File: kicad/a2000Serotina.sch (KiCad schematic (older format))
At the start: 23 parts

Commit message: Further work on Keyboard Matrix
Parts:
- added D13, D14, D15, D16, D17, D18, D19, D20, D21, D22, D23, D24, D25, D26, D27, D28, D29, D30, D31, D32, D33, D34, D35, D36, D37, D38, D39, D40, D41, D42, D43, D44, D45, D46, D47, D48, D49, D50, D51, D52, D53, D54, D55, D56, D57, D58, D59, D60, D61, D62, D63, D64, D65, D66, D67, D68, D69, D70, D8: D_Small, symbol Device:D_Small
- added MX13, MX14, MX15, MX16, MX17, MX18, MX19, MX20, MX21, MX22, MX23, MX24, MX25, MX26, MX27, MX28, MX29, MX30, MX31, MX32, MX33, MX34, MX35, MX36, MX37, MX38, MX39, MX40, MX41, MX42, MX43, MX44, MX45, MX46, MX47, MX48, MX49, MX50, MX51, MX52, MX53, MX54, MX55, MX56, MX57, MX58, MX59, MX60, MX61, MX62, MX63, MX64, MX65, MX66, MX67, MX68, MX69, MX70, MX8: MX-NoLED, symbol MX_Alps_Hybrid:MX-NoLED
- renumbered D9 to D10, D10 to D11, D11 to D12, D8 to D9, MX9 to MX10, MX10 to MX11, MX11 to MX12, MX8 to MX9
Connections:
- net COL0: no longer MX1.1 (COL)
- net ROW0: no longer D1.1 (K)
- net ROW1: no longer D2.1 (K)
- net ROW10: no longer D11.1 (K)
- net ROW11: no longer D12.1 (K)
- net ROW3: no longer D3.1 (K)
- net ROW4: no longer D4.1 (K)
- net ROW5: no longer D5.1 (K)
- net ROW6: no longer D6.1 (K)
- net ROW7: no longer D7.1 (K)
- net ROW8: no longer D9.1 (K)
- net ROW9: no longer D10.1 (K)
- new net: D13.2 (A), MX13.2 (ROW)
- new net: D14.2 (A), MX14.2 (ROW)
- new net: D15.2 (A), MX15.2 (ROW)
- new net: D16.2 (A), MX16.2 (ROW)
- new net: D17.2 (A), MX17.2 (ROW)
- new net: D19.2 (A), MX19.2 (ROW)
- new net: D20.2 (A), MX20.2 (ROW)
- new net: D21.2 (A), MX21.2 (ROW)
- new net: D22.2 (A), MX22.2 (ROW)
- new net: D25.2 (A), MX25.2 (ROW)
- new net: D24.2 (A), MX24.2 (ROW)
- new net: D23.2 (A), MX23.2 (ROW)
- new net: D26.2 (A), MX26.2 (ROW)
- new net: D27.2 (A), MX27.2 (ROW)
- new net: D28.2 (A), MX28.2 (ROW)
- new net: D29.2 (A), MX29.2 (ROW)
- new net: D30.2 (A), MX30.2 (ROW)
- new net: D31.2 (A), MX31.2 (ROW)
- new net: D18.2 (A), MX18.2 (ROW)
- new net: D8.2 (A), MX8.2 (ROW)
- new net: D32.2 (A), MX32.2 (ROW)
- new net: D33.2 (A), MX33.2 (ROW)
- new net: D34.2 (A), MX34.2 (ROW)
- new net: D35.2 (A), MX35.2 (ROW)
- new net: D36.2 (A), MX36.2 (ROW)
- new net: D37.2 (A), MX37.2 (ROW)
- new net: D38.2 (A), MX38.2 (ROW)
- new net: D39.2 (A), MX39.2 (ROW)
- new net: D40.2 (A), MX40.2 (ROW)
- new net: D41.2 (A), MX41.2 (ROW)
- new net: D42.2 (A), MX42.2 (ROW)
- new net: D43.2 (A), MX43.2 (ROW)
- new net: D44.2 (A), MX44.2 (ROW)
- new net: D45.2 (A), MX45.2 (ROW)
- new net: D46.2 (A), MX46.2 (ROW)
- new net: D47.2 (A), MX47.2 (ROW)
- new net: D48.2 (A), MX48.2 (ROW)
- new net: D49.2 (A), MX49.2 (ROW)
- new net: D50.2 (A), MX50.2 (ROW)
- new net: D51.2 (A), MX51.2 (ROW)
- new net: D52.2 (A), MX52.2 (ROW)
- new net: D53.2 (A), MX53.2 (ROW)
- new net: D54.2 (A), MX54.2 (ROW)
- new net: D55.2 (A), MX55.2 (ROW)
- new net: D56.2 (A), MX56.2 (ROW)
- new net: D57.2 (A), MX57.2 (ROW)
- new net: D58.2 (A), MX58.2 (ROW)
- new net: D59.2 (A), MX59.2 (ROW)
- new net: D60.2 (A), MX60.2 (ROW)
- new net: D61.2 (A), MX61.2 (ROW)
- new net: D62.2 (A), MX62.2 (ROW)
- new net: D63.2 (A), MX63.2 (ROW)
- new net: D64.2 (A), MX64.2 (ROW)
- new net: D65.2 (A), MX65.2 (ROW)
- new net: D66.2 (A), MX66.2 (ROW)
- new net: D67.2 (A), MX67.2 (ROW)
- new net: D68.2 (A), MX68.2 (ROW)
- new net: D69.2 (A), MX69.2 (ROW)
- new net: D70.2 (A), MX70.2 (ROW)
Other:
- moved on the sheet: D10, D11, D12, D7, D9, MX10, MX11, MX12, MX7, MX9

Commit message: Matrix now complete.
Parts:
- added D100, D101, D102, D103, D104, D105, D71, D72, D73, D74, D75, D76, D77, D78, D79, D80, D81, D82, D83, D84, D85, D86, D87, D88, D89, D90, D91, D92, D93, D94, D95, D96, D97, D98, D99: D_Small, symbol Device:D_Small
- added MX100, MX101, MX102, MX103, MX104, MX105, MX71, MX72, MX73, MX74, MX75, MX76, MX77, MX78, MX79, MX80, MX81, MX82, MX83, MX84, MX85, MX86, MX87, MX88, MX89, MX90, MX91, MX92, MX93, MX94, MX95, MX96, MX97, MX98, MX99: MX-NoLED, symbol MX_Alps_Hybrid:MX-NoLED
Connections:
- net COL0: now also MX1.1 (COL), MX10.1 (COL), MX11.1 (COL), MX12.1 (COL), MX2.1 (COL), MX3.1 (COL), MX4.1 (COL), MX5.1 (COL), MX6.1 (COL), MX7.1 (COL), MX8.1 (COL), MX9.1 (COL)
- net COL1: now also MX13.1 (COL), MX14.1 (COL), MX15.1 (COL), MX16.1 (COL), MX17.1 (COL), MX18.1 (COL), MX19.1 (COL), MX20.1 (COL), MX21.1 (COL), MX22.1 (COL)
- net COL10: now also MX104.1 (COL), MX105.1 (COL)
- net COL2: now also MX23.1 (COL), MX24.1 (COL), MX25.1 (COL), MX26.1 (COL), MX27.1 (COL), MX28.1 (COL), MX29.1 (COL), MX30.1 (COL), MX31.1 (COL), MX32.1 (COL), MX33.1 (COL), MX34.1 (COL)
- net COL3: now also MX35.1 (COL), MX36.1 (COL), MX37.1 (COL), MX38.1 (COL), MX39.1 (COL), MX40.1 (COL), MX41.1 (COL), MX42.1 (COL), MX43.1 (COL), MX44.1 (COL), MX45.1 (COL), MX46.1 (COL)
- net COL4: now also MX47.1 (COL), MX48.1 (COL), MX49.1 (COL), MX50.1 (COL), MX51.1 (COL), MX52.1 (COL), MX53.1 (COL), MX54.1 (COL), MX55.1 (COL), MX56.1 (COL), MX57.1 (COL), MX58.1 (COL)
- net COL5: now also MX59.1 (COL), MX60.1 (COL), MX61.1 (COL), MX62.1 (COL), MX63.1 (COL), MX64.1 (COL), MX65.1 (COL), MX66.1 (COL), MX67.1 (COL), MX68.1 (COL), MX69.1 (COL), MX70.1 (COL)
- net COL6: now also MX71.1 (COL), MX72.1 (COL), MX73.1 (COL), MX74.1 (COL), MX75.1 (COL), MX76.1 (COL), MX77.1 (COL), MX78.1 (COL), MX79.1 (COL)
- net COL7: now also MX80.1 (COL), MX81.1 (COL), MX82.1 (COL), MX83.1 (COL), MX84.1 (COL), MX85.1 (COL), MX86.1 (COL), MX87.1 (COL), MX88.1 (COL), MX89.1 (COL)
- net COL8: now also MX90.1 (COL), MX91.1 (COL), MX92.1 (COL), MX93.1 (COL), MX94.1 (COL), MX95.1 (COL)
- net COL9: now also MX100.1 (COL), MX101.1 (COL), MX102.1 (COL), MX103.1 (COL), MX98.1 (COL), MX99.1 (COL)
- net ROW0: now also D1.1 (K), D23.1 (K), D35.1 (K), D47.1 (K), D59.1 (K), D80.1 (K), D90.1 (K), D98.1 (K)
- net ROW1: now also D2.1 (K), D24.1 (K), D36.1 (K), D48.1 (K), D60.1 (K), D81.1 (K), D91.1 (K), D99.1 (K)
- net ROW10: now also D11.1 (K), D21.1 (K), D33.1 (K), D45.1 (K), D57.1 (K), D69.1 (K), D79.1 (K)
- net ROW11: now also D12.1 (K), D22.1 (K), D34.1 (K), D46.1 (K), D58.1 (K), D70.1 (K)
- net ROW2: now also D13.1 (K), D25.1 (K), D3.1 (K), D37.1 (K), D49.1 (K), D61.1 (K), D100.1 (K), D104.1 (K), D71.1 (K), D82.1 (K), D92.1 (K)
- net ROW3: now also D14.1 (K), D26.1 (K), D38.1 (K), D4.1 (K), D50.1 (K), D62.1 (K), D101.1 (K), D72.1 (K), D83.1 (K), D93.1 (K)
- net ROW4: now also D15.1 (K), D27.1 (K), D39.1 (K), D5.1 (K), D51.1 (K), D63.1 (K), D102.1 (K), D105.1 (K), D73.1 (K), D84.1 (K), D94.1 (K)
- net ROW5: now also D16.1 (K), D28.1 (K), D40.1 (K), D52.1 (K), D6.1 (K), D64.1 (K), D103.1 (K), D74.1 (K), D85.1 (K), D95.1 (K)
- net ROW6: now also D17.1 (K), D29.1 (K), D41.1 (K), D53.1 (K), D65.1 (K), D7.1 (K), D75.1 (K), D86.1 (K)
- net ROW7: now also D18.1 (K), D30.1 (K), D42.1 (K), D54.1 (K), D66.1 (K), D8.1 (K), D76.1 (K), D87.1 (K)
- net ROW8: now also D19.1 (K), D31.1 (K), D43.1 (K), D55.1 (K), D67.1 (K), D9.1 (K), D77.1 (K), D88.1 (K), D96.1 (K)
- net ROW9: now also D10.1 (K), D20.1 (K), D32.1 (K), D44.1 (K), D56.1 (K), D68.1 (K), D78.1 (K), D89.1 (K), D97.1 (K)
- new net: D71.2 (A), MX71.2 (ROW)
- new net: D72.2 (A), MX72.2 (ROW)
- new net: D73.2 (A), MX73.2 (ROW)
- new net: D74.2 (A), MX74.2 (ROW)
- new net: D75.2 (A), MX75.2 (ROW)
- new net: D76.2 (A), MX76.2 (ROW)
- new net: D77.2 (A), MX77.2 (ROW)
- new net: D78.2 (A), MX78.2 (ROW)
- new net: D79.2 (A), MX79.2 (ROW)
- new net: D80.2 (A), MX80.2 (ROW)
- new net: D81.2 (A), MX81.2 (ROW)
- new net: D82.2 (A), MX82.2 (ROW)
- new net: D83.2 (A), MX83.2 (ROW)
- new net: D84.2 (A), MX84.2 (ROW)
- new net: D85.2 (A), MX85.2 (ROW)
- new net: D86.2 (A), MX86.2 (ROW)
- new net: D87.2 (A), MX87.2 (ROW)
- new net: D88.2 (A), MX88.2 (ROW)
- new net: D89.2 (A), MX89.2 (ROW)
- new net: D90.2 (A), MX90.2 (ROW)
- new net: D91.2 (A), MX91.2 (ROW)
- new net: D92.2 (A), MX92.2 (ROW)
- new net: D93.2 (A), MX93.2 (ROW)
- new net: D94.2 (A), MX94.2 (ROW)
- new net: D95.2 (A), MX95.2 (ROW)
- new net: D96.2 (A), MX96.2 (ROW)
- new net: D97.2 (A), MX97.2 (ROW)
- new net: D98.2 (A), MX98.2 (ROW)
- new net: D99.2 (A), MX99.2 (ROW)
- new net: D100.2 (A), MX100.2 (ROW)
- new net: D101.2 (A), MX101.2 (ROW)
- new net: D102.2 (A), MX102.2 (ROW)
- new net: D103.2 (A), MX103.2 (ROW)
- new net: D104.2 (A), MX104.2 (ROW)
- new net: D105.2 (A), MX105.2 (ROW)
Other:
- moved on the sheet: D8, MX8

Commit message: Connections and wiring complete
Now working on PCB Footprints.
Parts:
- removed MX11, MX33, MX69: MX-NoLED, symbol MX_Alps_Hybrid:MX-NoLED
- added J1: KCDX-5S-S2, SamacSys_Parts:KCDX5SS2, symbol SamacSys_Parts:KCDX-5S-S2
- added LED1, LED2, LED3, LED4, LED5, LED6, LED7, LED8: LED, LED_THT:LED_D3.0mm, symbol Device:LED
- added MX11, MX33, MX69: MX-LED, symbol MX_Alps_Hybrid:MX-LED
- added R1, R10, R11, R12, R2, R3, R4, R5, R6, R7, R8, R9: 150, Resistor_THT:R_Axial_DIN0207_L6.3mm_D2.5mm_P10.16mm_Horizontal, symbol Device:R_Small
- D1, D10, D100, D101, D102, D103, D104, D105, D11, D12, D13, D14, D15, D16, D17, D18, D19, D2, D20, D21, D22, D23, D24, D25, D26, D27, D28, D29, D3, D30, D31, D32, D33, D34, D35, D36, D37, D38, D39, D4, D40, D41, D42, D43, D44, D45, D46, D47, D48, D49, D5, D50, D51, D52, D53, D54, D55, D56, D57, D58, D59, D6, D60, D61, D62, D63, D64, D65, D66, D67, D68, D69, D7, D70, D71, D72, D73, D74, D75, D76, D77, D78, D79, D8, D80, D81, D82, D83, D84, D85, D86, D87, D88, D89, D9, D90, D91, D92, D93, D94, D95, D96, D97, D98, D99: footprint (none) -> Diode_THT:D_DO-35_SOD27_P7.62mm_Horizontal
- U1: renamed from U?; footprint (none) -> teensy:Teensy2.0++
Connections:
- net COL0: now also MX11.1 (COL)
- net COL2: now also MX33.1 (COL)
- net COL5: now also MX69.1 (COL)
- net COL8: now also MX96.1 (COL), MX97.1 (COL)
- net CPLCK: now also R12.2
- net GND: now also MX7.4 (LEDGND), J1.5, LED1.1 (K), LED2.1 (K), LED3.1 (K), LED4.1 (K), LED5.1 (K), LED6.1 (K), LED7.1 (K), LED8.1 (K), MX11.4 (LEDGND), MX33.4 (LEDGND), MX69.4 (LEDGND)
- net KCLK: now also J1.3, R9.1
- net KDAT: now also J1.2, R10.1
- net NMLCK: now also R7.1
- net SCLCK: now also R8.1
- net STA1: now also R4.1
- net STA2: now also R5.1
- net STA3: now also R6.1
- net VCC: now also J1.4, R11.1
- net LCTRL: now reaches U1.11 (PE0)
- net LCTRL: now also R1.1
- net LALT: now reaches U1.12 (PE1)
- net LALT: now also R2.1
- net RGUI: now reaches U1.2 (PB7_OC0A_OC1C)
- net RGUI: now also R3.1
- net at MX7.3 (LED): now also R12.1
- net at D11.2 (A): now also MX11.2 (ROW)
- net at D33.2 (A): now also MX33.2 (ROW)
- net at D69.2 (A): now also MX69.2 (ROW)
- new net: MX11.3 (LED), R1.2
- new net: MX33.3 (LED), R2.2
- new net: MX69.3 (LED), R3.2
- new net: LED1.2 (A), R4.2
- new net: LED2.2 (A), R5.2
- new net: LED3.2 (A), R6.2
- new net: LED4.2 (A), R7.2
- new net: LED5.2 (A), R8.2
- new net: LED6.2 (A), R9.2
- new net: LED7.2 (A), R10.2
- new net: LED8.2 (A), R11.2

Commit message: All footprints now assigned
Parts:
- MX1, MX10, MX100, MX101, MX102, MX104, MX105, MX13, MX14, MX15, MX16, MX17, MX18, MX19, MX2, MX20, MX22, MX23, MX24, MX25, MX26, MX27, MX28, MX29, MX3, MX30, MX31, MX32, MX34, MX35, MX36, MX37, MX38, MX39, MX4, MX40, MX41, MX42, MX43, MX46, MX47, MX48, MX49, MX50, MX51, MX52, MX53, MX54, MX55, MX56, MX58, MX59, MX6, MX60, MX61, MX62, MX63, MX64, MX65, MX66, MX67, MX68, MX70, MX71, MX72, MX73, MX74, MX75, MX76, MX77, MX78, MX8, MX80, MX81, MX82, MX83, MX84, MX85, MX86, MX87, MX88, MX89, MX90, MX91, MX92, MX93, MX94, MX95, MX96, MX98, MX99: footprint (none) -> MX_Alps_Hybrid:MX-1U-NoLED
- MX103, MX97: footprint (none) -> MX_Alps_Hybrid:MX-2U-NoLED
- MX11, MX33, MX69: footprint (none) -> MX_Alps_Hybrid:MX-1.25U
- MX12, MX21, MX57, MX79, MX9: footprint (none) -> MX_Alps_Hybrid:MX-1.25U-NoLED
- MX44: footprint (none) -> MX_Alps_Hybrid:MX-2.75U-NoLED
- MX45: footprint (none) -> MX_Alps_Hybrid:MX-6.25U-NoLED
- MX5: footprint (none) -> MX_Alps_Hybrid:MX-1.5U-NoLED
- MX7: footprint (none) -> MX_Alps_Hybrid:MX-1.75U

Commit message: Work on PCB Layout
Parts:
- MX26, MX28: footprint MX_Alps_Hybrid:MX-1U-NoLED -> MX_Alps_Hybrid:MX-2U-NoLED
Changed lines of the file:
@@
 F 0 "MX26" H 3383 4071 60  0000 C CNN
 F 1 "MX-NoLED" H 3383 3949 20  0001 C CNN
-F 2 "MX_Alps_Hybrid:MX-1U-NoLED" H 2725 3775 60  0001 C CNN
+F 2 "MX_Alps_Hybrid:MX-2U-NoLED" H 2725 3775 60  0001 C CNN
 F 3 "" H 2725 3775 60  0001 C CNN
 F 4 "BSPC" H 3383 3973 50  0000 C CNN "Key"
@@
 F 0 "MX28" H 3383 5471 60  0000 C CNN
 F 1 "MX-NoLED" H 3383 5349 20  0001 C CNN
-F 2 "MX_Alps_Hybrid:MX-1U-NoLED" H 2725 5175 60  0001 C CNN
+F 2 "MX_Alps_Hybrid:MX-2U-NoLED" H 2725 5175 60  0001 C CNN
 F 3 "" H 2725 5175 60  0001 C CNN
 F 4 "ENT" H 3383 5373 50  0000 C CNN "Key"

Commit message: All switches now placed.
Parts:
- MX58: footprint MX_Alps_Hybrid:MX-1U-NoLED -> MX_Alps_Hybrid:MX-2U-NoLED
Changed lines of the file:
@@
 F 0 "MX58" H 4383 9671 60  0000 C CNN
 F 1 "MX-NoLED" H 4383 9549 20  0001 C CNN
-F 2 "MX_Alps_Hybrid:MX-1U-NoLED" H 3725 9375 60  0001 C CNN
+F 2 "MX_Alps_Hybrid:MX-2U-NoLED" H 3725 9375 60  0001 C CNN
 F 3 "" H 3725 9375 60  0001 C CNN
 F 4 "P0" H 4383 9573 50  0000 C CNN "Key"

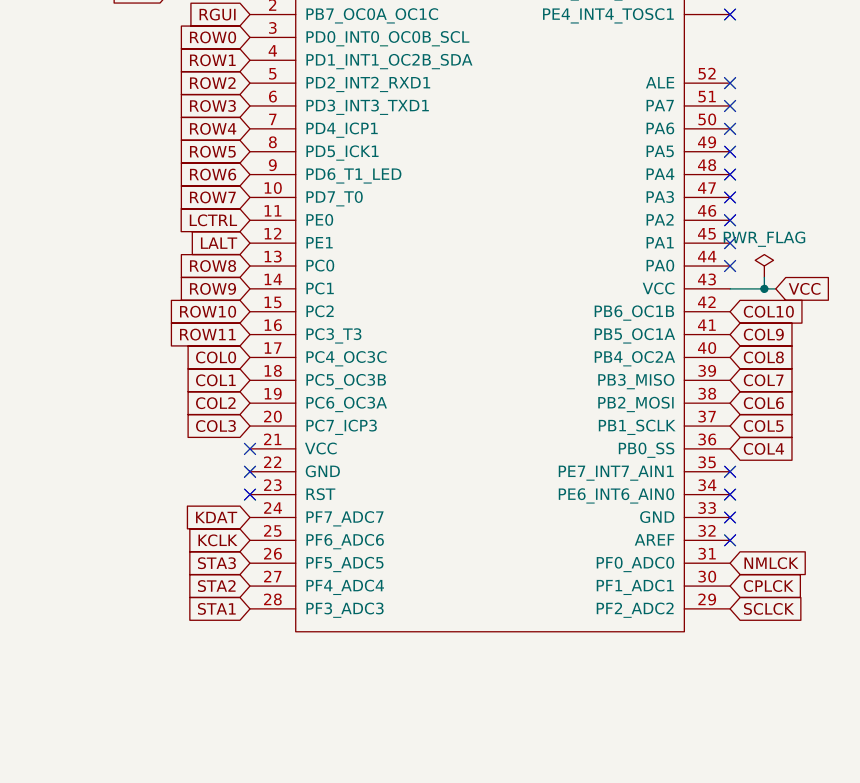
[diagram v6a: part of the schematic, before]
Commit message: Change Row 6 Pin from D6 to F2
D6 lights the LED on the Teensy 2.0 ++ - better to have D6 control a LED.
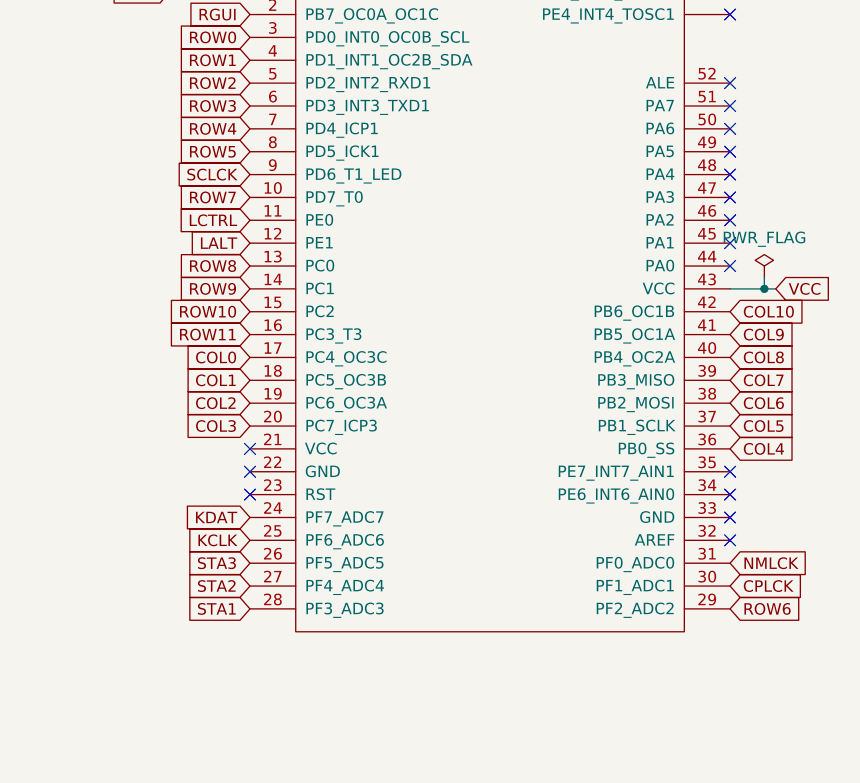
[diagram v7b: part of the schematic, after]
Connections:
- net ROW6: now also U1.29 (PF2_ADC2); no longer U1.9 (PD6_T1_LED)
- net SCLCK: now also U1.9 (PD6_T1_LED); no longer U1.29 (PF2_ADC2)
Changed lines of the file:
@@
 Text GLabel 18300 2600 0    50   Input ~ 0
 ROW5
-Text GLabel 18300 2700 0    50   Input ~ 0
+Text GLabel 20400 4600 2    50   Input ~ 0
 ROW6
 Text GLabel 18300 2800 0    50   Input ~ 0
@@
 Text GLabel 20400 4500 2    50   Input ~ 0
 CPLCK
-Text GLabel 20400 4600 2    50   Input ~ 0
+Text GLabel 18300 2700 0    50   Input ~ 0
 SCLCK
 Text GLabel 18300 4300 0    50   Input ~ 0

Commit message: Updated column / row layout of switches
Now much more regular on the bottom rows.
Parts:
- MX10: Key LABK -> COMM
- MX19: Key BSLS -> NUBS
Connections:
- net COL0: now also MX32.1 (COL), MX36.1 (COL), MX42.1 (COL), MX69.1 (COL), U1.31 (PF0_ADC0); no longer MX10.1 (COL), MX12.1 (COL), MX2.1 (COL), MX8.1 (COL), U1.17 (PC4_OC3C)
- net COL1: now also MX44.1 (COL), MX48.1 (COL), MX54.1 (COL), MX79.1 (COL), U1.30 (PF1_ADC1); no longer MX18.1 (COL), MX20.1 (COL), MX22.1 (COL), U1.18 (PC5_OC3B)
- net COL10: now also MX20.1 (COL), MX24.1 (COL), MX30.1 (COL), MX57.1 (COL), U1.20 (PC7_ICP3); no longer U1.42 (PB6_OC1B)
- net COL2: now also MX12.1 (COL), MX60.1 (COL), U1.29 (PF2_ADC2); no longer MX24.1 (COL), MX30.1 (COL), MX32.1 (COL), MX34.1 (COL), U1.19 (PC6_OC3A)
- net COL3: now also MX22.1 (COL), MX81.1 (COL), U1.13 (PC0); no longer MX36.1 (COL), MX42.1 (COL), MX44.1 (COL), MX45.1 (COL), MX46.1 (COL), U1.20 (PC7_ICP3)
- net COL4: now also MX34.1 (COL), MX91.1 (COL), U1.14 (PC1); no longer MX48.1 (COL), MX54.1 (COL), MX57.1 (COL), MX58.1 (COL), U1.36 (PB0_SS)
- net COL5: now also MX46.1 (COL), MX99.1 (COL), U1.15 (PC2); no longer MX60.1 (COL), MX66.1 (COL), MX68.1 (COL), MX69.1 (COL), MX70.1 (COL), U1.37 (PB1_SCLK)
- net COL6: now also MX45.1 (COL), MX58.1 (COL), MX66.1 (COL), MX68.1 (COL), MX80.1 (COL), U1.16 (PC3_T3); no longer MX76.1 (COL), MX78.1 (COL), MX79.1 (COL), U1.38 (PB2_MOSI)
- net COL7: now also MX76.1 (COL), MX78.1 (COL), MX90.1 (COL), U1.17 (PC4_OC3C); no longer MX80.1 (COL), MX81.1 (COL), MX87.1 (COL), MX89.1 (COL), U1.39 (PB3_MISO)
- net COL8: now also MX70.1 (COL), MX8.1 (COL), MX87.1 (COL), MX89.1 (COL), MX98.1 (COL), U1.18 (PC5_OC3B); no longer MX90.1 (COL), MX91.1 (COL), MX97.1 (COL), U1.40 (PB4_OC2A)
- net COL9: now also MX10.1 (COL), MX18.1 (COL), MX2.1 (COL), MX97.1 (COL), U1.19 (PC6_OC3A); no longer MX98.1 (COL), MX99.1 (COL), U1.41 (PB5_OC1A)
- net CPLCK: now also U1.10 (PD7_T0); no longer U1.30 (PF1_ADC1)
- net NMLCK: now also U1.8 (PD5_ICK1); no longer U1.31 (PF0_ADC0)
- net ROW0: now also D2.1 (K), D24.1 (K), U1.36 (PB0_SS); no longer U1.3 (PD0_INT0_OC0B_SCL)
- net ROW1: now also U1.37 (PB1_SCLK); no longer D2.1 (K), D24.1 (K), U1.4 (PD1_INT1_OC2B_SDA)
- net ROW10: now also U1.42 (PB6_OC1B); no longer D69.1 (K), D79.1 (K), U1.15 (PC2)
- net ROW11: now also D69.1 (K), D79.1 (K), U1.7 (PD4_ICP1); no longer U1.16 (PC3_T3)
- net ROW2: now also U1.38 (PB2_MOSI); no longer U1.5 (PD2_INT2_RXD1)
- net ROW3: now also U1.3 (PD0_INT0_OC0B_SCL); no longer U1.6 (PD3_INT3_TXD1)
- net ROW4: now also U1.39 (PB3_MISO); no longer U1.7 (PD4_ICP1)
- net ROW5: now also U1.4 (PD1_INT1_OC2B_SDA); no longer U1.8 (PD5_ICK1)
- net ROW6: now also D18.1 (K), D30.1 (K), D8.1 (K), U1.40 (PB4_OC2A); no longer U1.29 (PF2_ADC2)
- net ROW7: now also U1.5 (PD2_INT2_RXD1); no longer D18.1 (K), D30.1 (K), D8.1 (K), U1.10 (PD7_T0)
- net ROW8: now also D10.1 (K), D20.1 (K), U1.41 (PB5_OC1A); no longer U1.13 (PC0)
- net ROW9: now also U1.6 (PD3_INT3_TXD1); no longer D10.1 (K), D20.1 (K), U1.14 (PC1)
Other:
- moved on the sheet: D10, D12, D18, D2, D20, D22, D24, D30, D32, D34, D36, D42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
